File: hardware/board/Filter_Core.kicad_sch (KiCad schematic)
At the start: 51 parts, among them U3 TL074

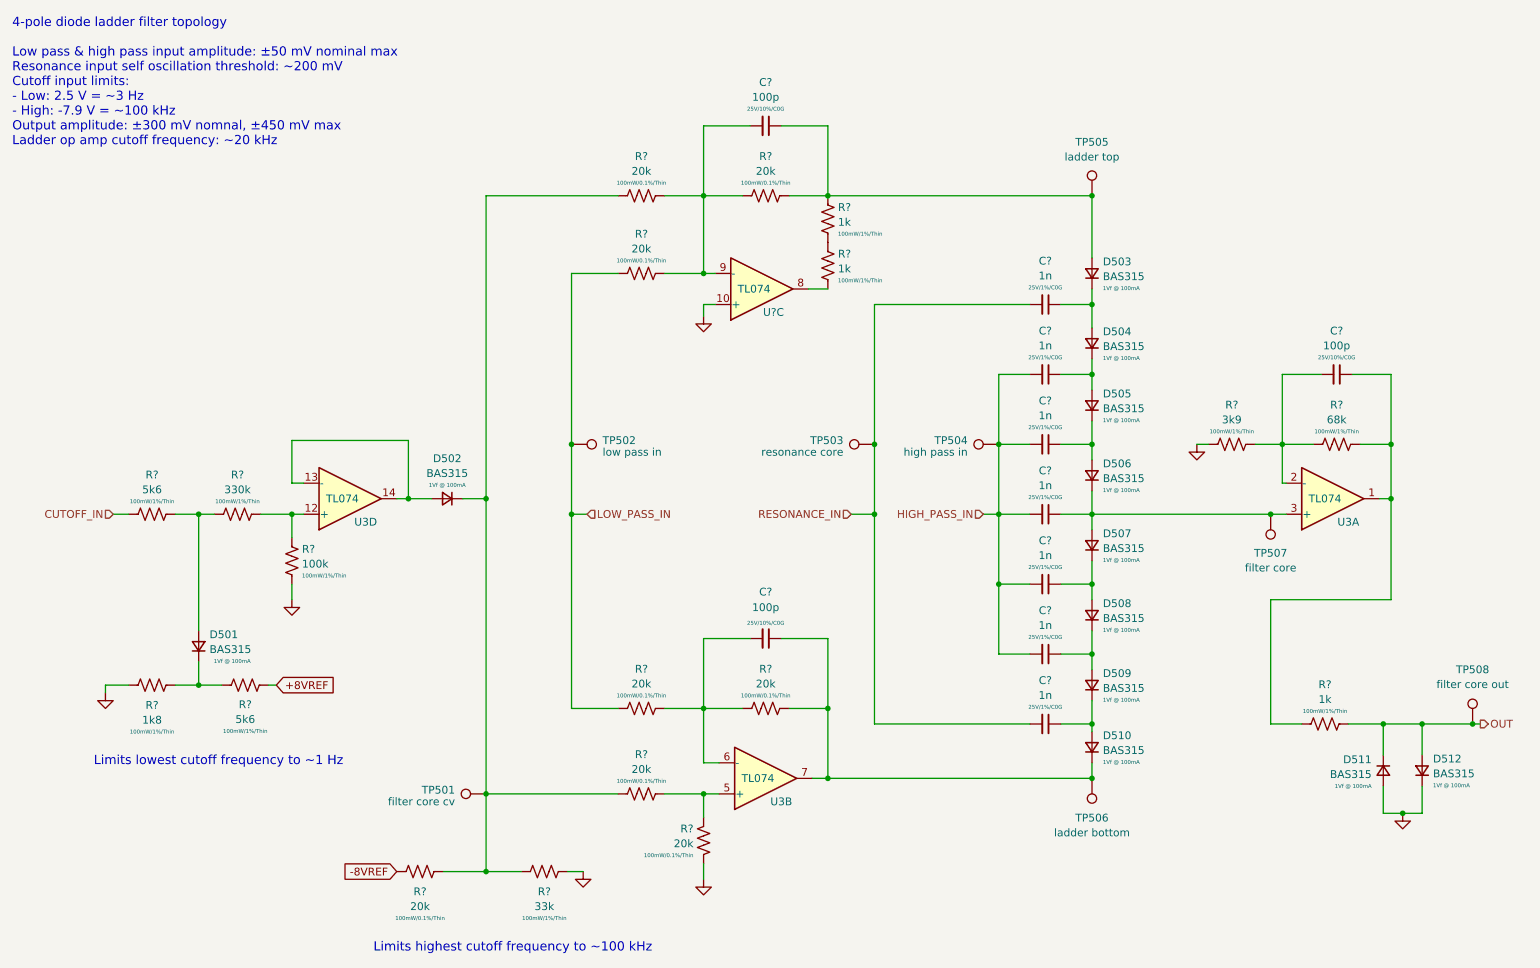
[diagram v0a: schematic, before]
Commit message: update board to kicad 9
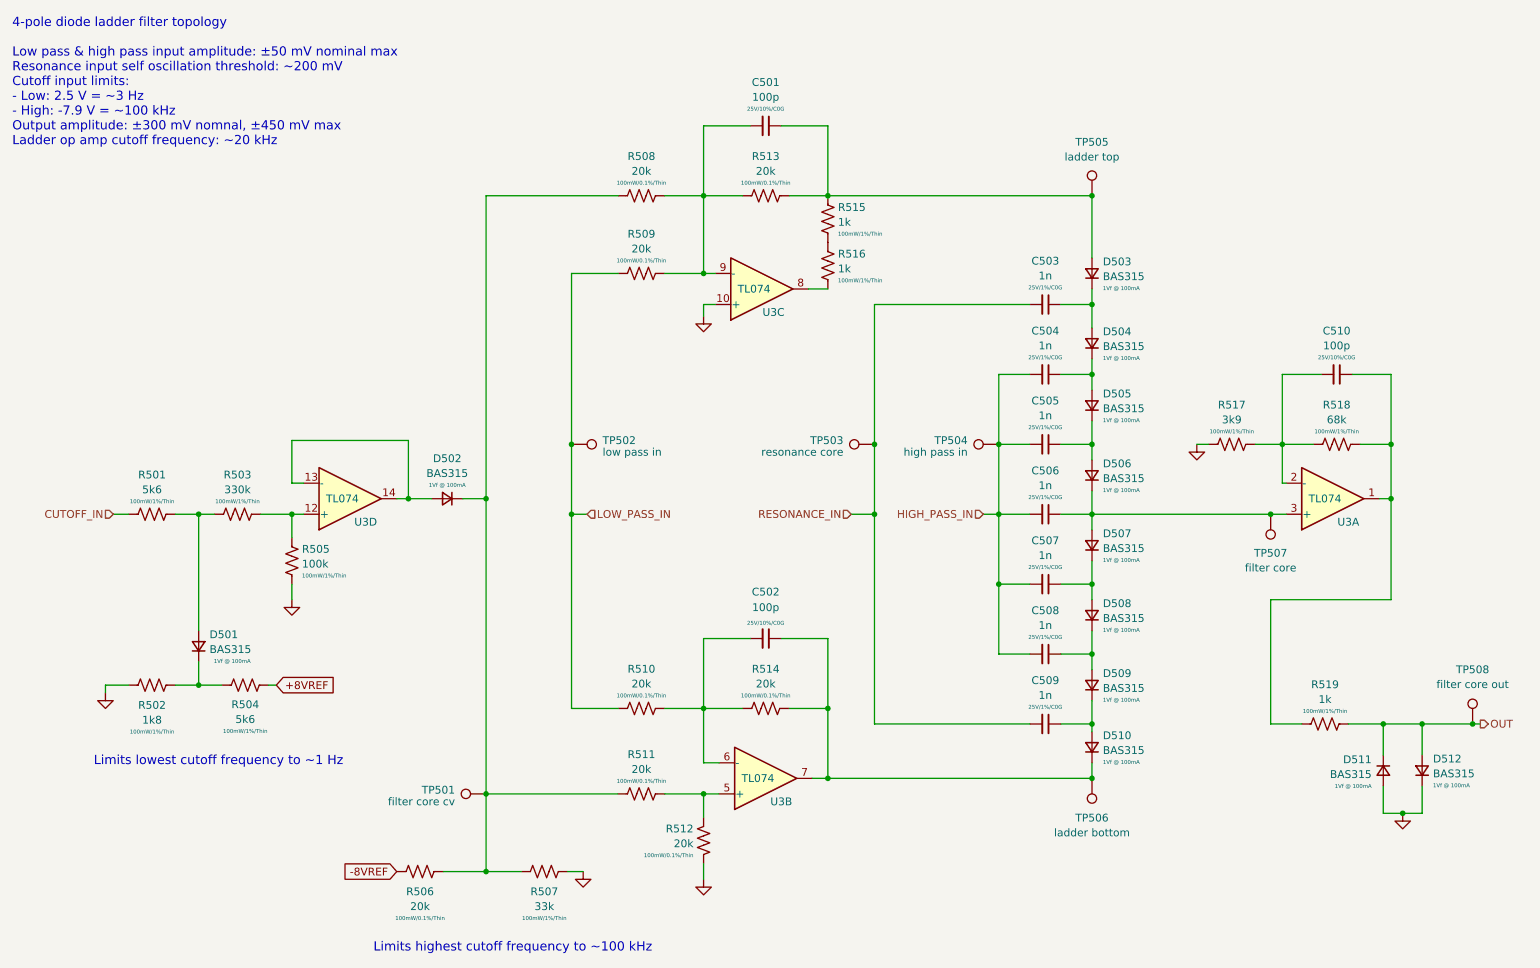
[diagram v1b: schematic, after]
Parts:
- gave numbers to parts that had none: 30

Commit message: remove test points from BOM
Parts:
- TP501, TP502, TP503, TP504, TP505, TP506, TP507, TP508: now left out of the parts list
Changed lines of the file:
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@@
 		(unit 1)
 		(exclude_from_sim no)
-		(in_bom yes)
+		(in_bom no)
 		(on_board yes)
 		(dnp no)
@@
 		(unit 1)
 		(exclude_from_sim no)
-		(in_bom yes)
+		(in_bom no)
 		(on_board yes)
 		(dnp no)
@@
 		(unit 1)
 		(exclude_from_sim no)
-		(in_bom yes)
+		(in_bom no)
 		(on_board yes)
 		(dnp no)
@@
 		(unit 1)
 		(exclude_from_sim no)
-		(in_bom yes)
+		(in_bom no)
 		(on_board yes)
 		(dnp no)
@@
 		(unit 1)
 		(exclude_from_sim no)
-		(in_bom yes)
+		(in_bom no)
 		(on_board yes)
 		(dnp no)
@@
 		(unit 1)
 		(exclude_from_sim no)
-		(in_bom yes)
+		(in_bom no)
 		(on_board yes)
 		(dnp no)
@@
 		(unit 1)
 		(exclude_from_sim no)
-		(in_bom yes)
+		(in_bom no)
 		(on_board yes)
 		(dnp no)
@@
 		(unit 1)
 		(exclude_from_sim no)
-		(in_bom yes)
+		(in_bom no)
 		(on_board yes)
 		(dnp no)
